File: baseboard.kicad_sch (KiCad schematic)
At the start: 50 parts, among them J10 LCD_CHAR, J11 SERVO2, J12 BME280, J13 UART1, J14 FAN, J15 UART2, J16 AS7265X, J17 TFT_SPI, J5 POWER, J6 DCMI_CAMERA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

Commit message: snapshot
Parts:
- removed J17: TFT_SPI, Connector_PinHeader_2.54mm:PinHeader_1x15_P2.54mm_Vertical, symbol EggClassifier:Conn_01x15
- added J17: TFT_SPI, EggClassifier:PinSocket_1x14_P2.54mm_Vertical, symbol LM2676S-3.3_NOPB:Conn_01x14
- C1, C3, C4: footprint Capacitor_THT:CP_Radial_D8.0mm_P3.50mm -> EggClassifier:CP_Radial_D8.0mm_P3.50mm_Hole1.0mm
- C10, C11, C2, C5, C6, C7, C8, C9: footprint Capacitor_SMD:C_0805_2012Metric_Pad1.18x1.45mm_HandSolder -> EggClassifier:C_0805_2012Metric_Pad1.18x1.45mm_HandSolder
- D1: footprint Diode_SMD:D_SMB_Handsoldering -> EggClassifier:D_SMB_Handsoldering
- D2, D3, D4: footprint Diode_SMD:D_SMA_Handsoldering -> EggClassifier:D_SMA_Handsoldering
- D5: footprint LED_SMD:LED_0805_2012Metric_Pad1.15x1.40mm_HandSolder -> EggClassifier:LED_0805_2012Metric_Pad1.15x1.40mm_HandSolder
- H1, H2, H3, H4: footprint PCM_JLCPCB:Hole, 3mm -> EggClassifier:Hole, 3mm
- J10, J12, J16, J5: footprint Connector_PinHeader_2.54mm:PinHeader_1x04_P2.54mm_Vertical -> EggClassifier:PinHeader_1x04_P2.54mm_Vertical
- J11, J13, J14, J15, J8, J9: footprint Connector_PinHeader_2.54mm:PinHeader_1x03_P2.54mm_Vertical -> EggClassifier:PinHeader_1x03_P2.54mm_Vertical
- J6: footprint Connector_PinHeader_2.54mm:PinHeader_2x09_P2.54mm_Vertical -> EggClassifier:PinHeader_2x09_P2.54mm_Vertical
- J7: footprint Connector_PinHeader_2.54mm:PinHeader_2x05_P2.54mm_Vertical -> EggClassifier:PinHeader_2x05_P2.54mm_Vertical
- L1: footprint JLCPCB:L_SMD,8x8mm -> EggClassifier:L_SMD,8x8mm
- Q1, Q2, Q3: footprint PCM_Package_TO_SOT_SMD_AKL:SOT-223-3_TabPin2 -> EggClassifier:SOT-223-3_TabPin2
- R1, R10, R11, R2, R3, R4, R5, R6, R7, R8, R9: footprint Resistor_SMD:R_0805_2012Metric_Pad1.20x1.40mm_HandSolder -> EggClassifier:R_0805_2012Metric_Pad1.20x1.40mm_HandSolder
- U1: footprint LM2676S-3.3_NOPB:TO127P1435X464-8N -> EggClassifier:TO127P1435X464-8N
- U2: footprint Package_TO_SOT_SMD:SOT-223-3_TabPin2 -> EggClassifier:SOT-223-3_TabPin2
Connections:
- net GND: now also J17.2 (Pin_2); no longer J7.9 (Pin_9)
- net SPI1_MISO: now also J17.13 (Pin_13)
- net SPI1_MOSI: now also J17.12 (Pin_12)
- net SPI1_NCS: now also J17.11 (Pin_11)
- net SPI1_SCK: now also J17.10 (Pin_10)
- net SPI2_MISO: now also J17.9 (Pin_9)
- net SPI2_MOSI: now also J17.6 (Pin_6)
- net SPI2_NCS: now also J17.3 (Pin_3)
- net SPI2_SCK: now also J17.7 (Pin_7)
- net TFT_BL: now also J17.8 (Pin_8)
- net TFT_INT: now also J17.14 (Pin_14)
- net TFT_RS: now also J17.5 (Pin_5)
- net VCC: now also J7.9 (Pin_9), J17.1 (Pin_1)
- net at R11.2: now also J17.4 (Pin_4)

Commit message: yet more tweaks
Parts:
- J5: footprint EggClassifier:PinHeader_1x04_P2.54mm_Vertical -> EggClassifier:TerminalBlock_Xinya_XY308-2.54-4P_1x04_P2.54mm_Horizontal
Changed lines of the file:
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@@
 			)
 		)
-		(property "Footprint" "EggClassifier:PinHeader_1x04_P2.54mm_Vertical"
+		(property "Footprint" "EggClassifier:TerminalBlock_Xinya_XY308-2.54-4P_1x04_P2.54mm_Horizontal"
 			(at 25.4 133.35 0)
 			(effects

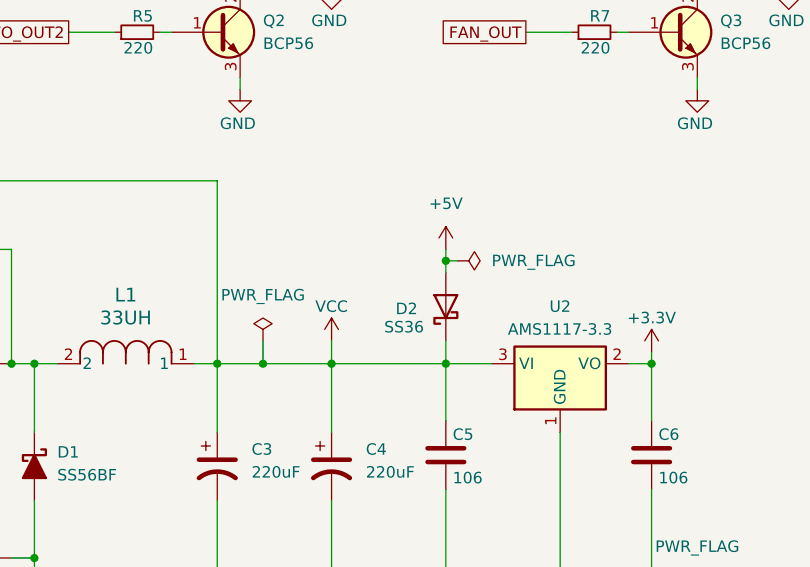
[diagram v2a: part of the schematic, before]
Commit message: change board to dimensions 120mm x 80mm
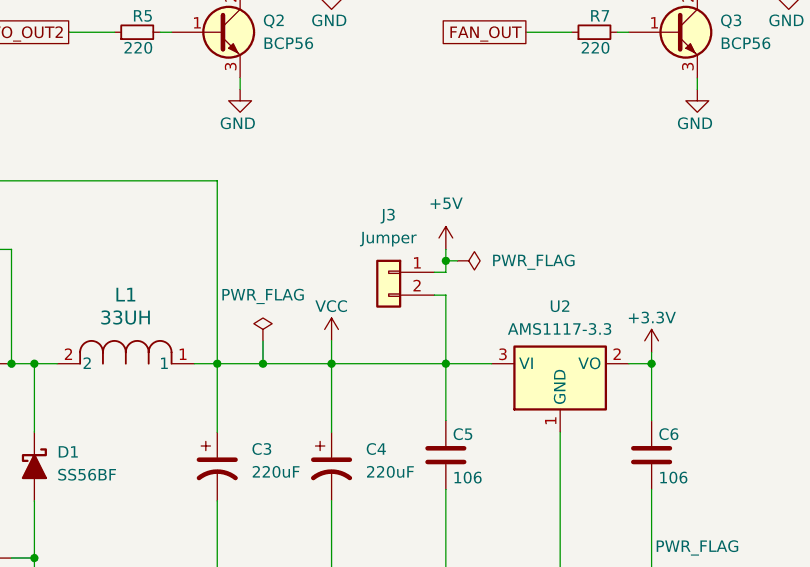
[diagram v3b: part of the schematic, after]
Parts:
- removed D2: SS36, EggClassifier:D_SMA_Handsoldering, symbol EggClassifier:SS36
- added J3: Jumper, Connector_PinSocket_2.54mm:PinSocket_1x02_P2.54mm_Vertical, symbol Connector_Generic:Conn_01x02
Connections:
- net +5V: now also J3.1 (Pin_1)
- net VCC: now also J3.2 (Pin_2)
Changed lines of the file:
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@@
 	(wire
 		(pts
+			(xy 144.78 125.73) (xy 146.05 125.73)
+		)
+		(stroke
+			(width 0)
+			(type default)
+		)
+	)
+	(wire
+		(pts
 			(xy 190.5 62.23) (xy 191.77 62.23)
 		)
@@
 	(wire
 		(pts
+			(xy 144.78 128.27) (xy 146.05 128.27)
+		)
+		(stroke
+			(width 0)
+			(type default)
+		)
+	)
+	(wire
+		(pts
 			(xy 190.5 24.13) (xy 190.5 25.4)
 		)
@@
 	(wire
 		(pts
-			(xy 146.05 133.35) (xy 146.05 135.89)
+			(xy 146.05 128.27) (xy 146.05 135.89)
 		)
 		(stroke
@@
 	)
 	(symbol
-		(lib_id "EggClassifier:SS36")
-		(at 146.05 129.54 90)
-		(unit 1)
-		(exclude_from_sim no)
-		(in_bom yes)
-		(on_board yes)
-		(dnp no)
-		(property "Reference" "D2"
-			(at 140.462 129.794 90)
-			(effects
-				(font
-					(size 1.27 1.27)
-				)
-				(justify right)
-			)
-		)
-		(property "Value" "SS36"
-			(at 139.192 131.826 90)
-			(effects
-				(font
-					(size 1.27 1.27)
-				)
-				(justify right)
-			)
-		)
-		(property "Footprint" "EggClassifier:D_SMA_Handsoldering"
-			(at 150.495 129.54 0)
-			(effects
-				(font
-					(size 1.27 1.27)
-				)
-				(hide yes)
-			)
-		)
-		(property "Datasheet" "https://www.vishay.com/docs/88751/ss32.pdf"
-			(at 146.05 129.54 0)
-			(effects
-				(font
-					(size 1.27 1.27)
-				)
-				(hide yes)
-			)
-		)
-		(property "Description" "60V 3A Schottky Diode, SMA"
-			(at 146.05 129.54 0)
-			(effects
-				(font
-					(size 1.27 1.27)
-				)
-				(hide yes)
-			)
-		)
-		(pin "1"
-		)
-		(pin "2"
-		)
-		(instances
-			(project "Main_H743VI"
-				(path "/1c72d2eb-7fb1-49fe-a026-e817f5a7ec43/16aff487-3924-4be3-b176-d1fab0e3868e"
-					(reference "D2")
-					(unit 1)
-				)
-			)
-		)
-	)
-	(symbol
 		(lib_id "EggClassifier:Conn_01x03")
 		(at 196.85 62.23 0)
@@
 					(unit 1)
 				)
+			)
+		)
+	)
+	(symbol
+		(lib_id "Connector_Generic:Conn_01x02")
+		(at 139.7 125.73 0)
+		(mirror y)
+		(unit 1)
+		(exclude_from_sim no)
+		(in_bom yes)
+		(on_board yes)
+		(dnp no)
+		(fields_autoplaced yes)
+		(property "Reference" "J3"
+			(at 139.7 119.38 0)
+			(effects
+				(font
+					(size 1.27 1.27)
+				)
+			)
+		)
+		(property "Value" "Jumper"
+			(at 139.7 121.92 0)
+			(effects
+				(font
+					(size 1.27 1.27)
+				)
+			)
+		)
+		(property "Footprint" "Connector_PinSocket_2.54mm:PinSocket_1x02_P2.54mm_Vertical"
+			(at 139.7 125.73 0)
+			(effects
+				(font
+					(size 1.27 1.27)
+				)
+				(hide yes)
+			)
+		)
+		(property "Datasheet" "~"
+			(at 139.7 125.73 0)
+			(effects
+				(font
+					(size 1.27 1.27)
+				)
+				(hide yes)
+			)
+		)
+		(property "Description" "Generic connector, single row, 01x02, script generated (kicad-library-utils/schlib/autogen/connector/)"
+			(at 139.7 125.73 0)
+			(effects
+				(font
+					(size 1.27 1.27)
+				)
+				(hide yes)
+			)
+		)
+		(pin "1"
+		)
+		(pin "2"
+		)
+		(instances
+			(project ""
+				(path "/1c72d2eb-7fb1-49fe-a026-e817f5a7ec43/16aff487-3924-4be3-b176-d1fab0e3868e"
+					(reference "J3")
+					(unit 1)
+				)

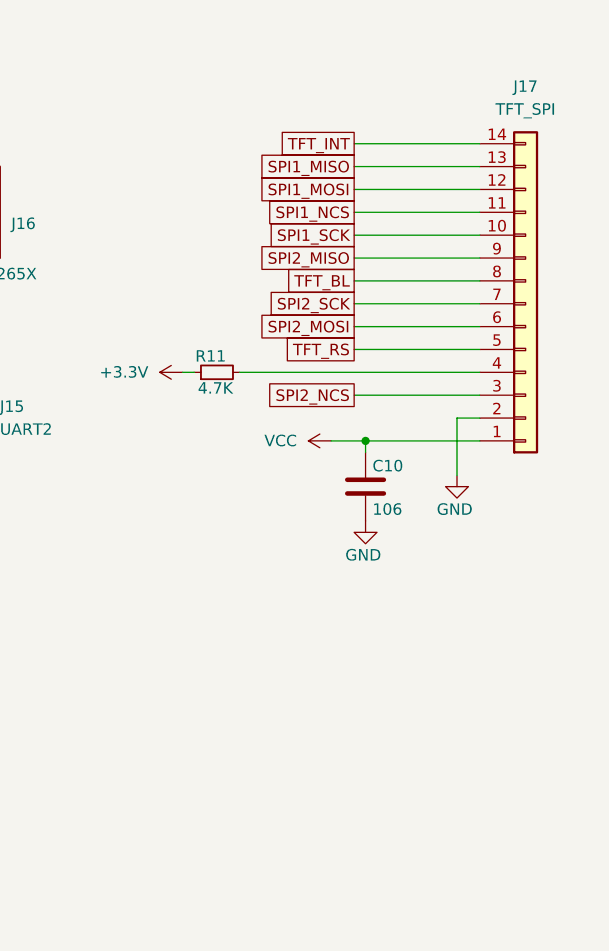
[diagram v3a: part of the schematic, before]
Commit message: finished layout;. H743 with SD-Card
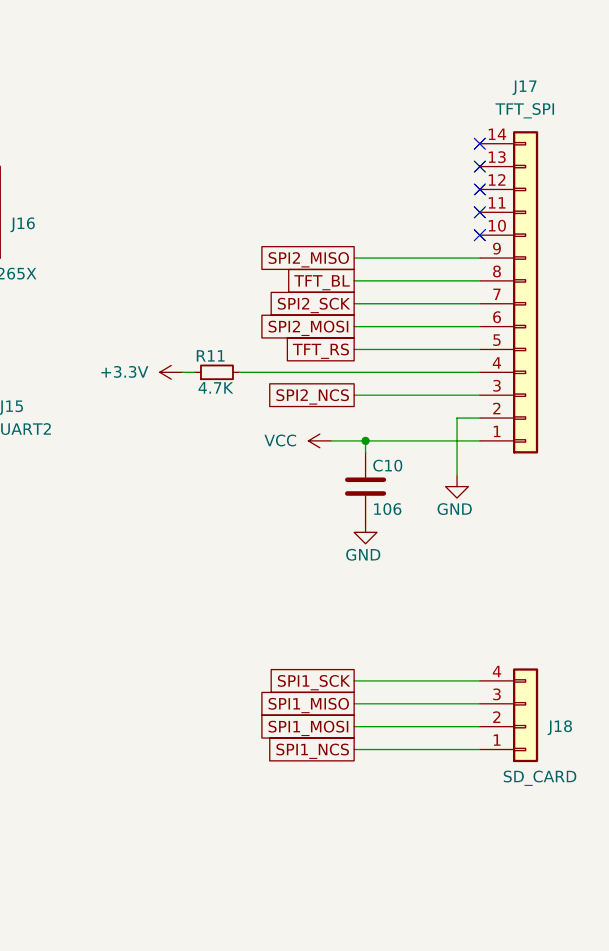
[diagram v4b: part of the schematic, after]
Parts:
- added J18: SD_CARD, EggClassifier:PinHeader_1x04_P2.54mm_Vertical, symbol EggClassifier:Conn_01x04
- J3: footprint Connector_PinSocket_2.54mm:PinSocket_1x02_P2.54mm_Vertical -> Connector_PinHeader_2.54mm:PinHeader_1x02_P2.54mm_Vertical
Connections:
- net SPI1_MISO: now also J18.3 (Pin_3); no longer J17.13 (Pin_13)
- net SPI1_MOSI: now also J18.2 (Pin_2); no longer J17.12 (Pin_12)
- net SPI1_NCS: now also J18.1 (Pin_1); no longer J17.11 (Pin_11)
- net SPI1_SCK: now also J18.4 (Pin_4); no longer J17.10 (Pin_10)
- net TFT_INT: no longer names the net of J17.14 (Pin_14)
- no-connect marks 2 -> 7
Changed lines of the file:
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@@
 	)
 	(no_connect
+		(at 252.73 39.37)
+	)
+	(no_connect
+		(at 252.73 36.83)
+	)
+	(no_connect
 		(at 62.23 151.13)
 	)
@@
 		(at 62.23 156.21)
 	)
+	(no_connect
+		(at 252.73 31.75)
+	)
+	(no_connect
+		(at 252.73 34.29)
+	)
+	(no_connect
+		(at 252.73 41.91)
+	)
 	(wire
 		(pts
@@
 	(wire
 		(pts
-			(xy 252.73 41.91) (xy 238.76 41.91)
+			(xy 252.73 91.44) (xy 238.76 91.44)
 		)
 		(stroke
@@
 	(wire
 		(pts
-			(xy 252.73 31.75) (xy 238.76 31.75)
-		)
-		(stroke
-			(width 0)
-			(type default)
-		)
-	)
-	(wire
-		(pts
 			(xy 173.99 83.82) (xy 184.15 83.82)
 		)
@@
 	(wire
 		(pts
-			(xy 252.73 36.83) (xy 238.76 36.83)
+			(xy 252.73 96.52) (xy 238.76 96.52)
 		)
 		(stroke
@@
 	(wire
 		(pts
-			(xy 252.73 34.29) (xy 238.76 34.29)
+			(xy 252.73 93.98) (xy 238.76 93.98)
 		)
 		(stroke
@@
 	(wire
 		(pts
-			(xy 252.73 39.37) (xy 238.76 39.37)
+			(xy 252.73 99.06) (xy 238.76 99.06)
 		)
 		(stroke
@@
 	(global_label "SPI1_MISO"
 		(shape passive)
-		(at 238.76 34.29 180)
+		(at 238.76 93.98 180)
 		(fields_autoplaced yes)
 		(effects
@@
 		)
 		(property "Intersheetrefs" "${INTERSHEET_REFS}"
-			(at 227.0285 34.29 0)
+			(at 227.0285 93.98 0)
 			(effects
 				(font
@@
 	(global_label "SPI1_SCK"
 		(shape passive)
-		(at 238.76 41.91 180)
+		(at 238.76 91.44 180)
 		(fields_autoplaced yes)
 		(effects
@@
 		)
 		(property "Intersheetrefs" "${INTERSHEET_REFS}"
-			(at 227.8752 41.91 0)
+			(at 227.8752 91.44 0)
 			(effects
 				(font
@@
 	(global_label "SPI1_MOSI"
 		(shape passive)
-		(at 238.76 36.83 180)
+		(at 238.76 96.52 180)
 		(fields_autoplaced yes)
 		(effects
@@
 		)
 		(property "Intersheetrefs" "${INTERSHEET_REFS}"
-			(at 227.0285 36.83 0)
+			(at 227.0285 96.52 0)
 			(effects
 				(font
@@
 		)
 	)
-	(global_label "TFT_INT"
-		(shape passive)
-		(at 238.76 31.75 180)
-		(fields_autoplaced yes)
-		(effects
-			(font
-				(size 1.27 1.27)
-			)
-			(justify right)
-		)
-		(property "Intersheetrefs" "${INTERSHEET_REFS}"
-			(at 229.9918 31.75 0)
-			(effects
-				(font
-					(size 1.27 1.27)
-				)
-				(justify right)
-				(hide yes)
-			)
-		)
-	)
 	(global_label "TFT_RS"
 		(shape passive)
@@
 	(global_label "SPI1_NCS"
 		(shape passive)
-		(at 238.76 39.37 180)
+		(at 238.76 99.06 180)
 		(fields_autoplaced yes)
 		(effects
@@
 		)
 		(property "Intersheetrefs" "${INTERSHEET_REFS}"
-			(at 227.8147 39.37 0)
+			(at 227.8147 99.06 0)
 			(effects
 				(font
@@
 	)
 	(symbol
+		(lib_id "EggClassifier:Conn_01x04")
+		(at 257.81 96.52 0)
+		(mirror x)
+		(unit 1)
+		(exclude_from_sim no)
+		(in_bom yes)
+		(on_board yes)
+		(dnp no)
+		(property "Reference" "J18"
+			(at 260.35 96.5201 0)
+			(effects
+				(font
+					(size 1.27 1.27)
+				)
+				(justify left)
+			)
+		)
+		(property "Value" "SD_CARD"
+			(at 255.27 102.108 0)
+			(effects
+				(font
+					(size 1.27 1.27)
+				)
+				(justify left)
+			)
+		)
+		(property "Footprint" "EggClassifier:PinHeader_1x04_P2.54mm_Vertical"
+			(at 257.81 96.52 0)
+			(effects
+				(font
+					(size 1.27 1.27)
+				)
+				(hide yes)
+			)
+		)
+		(property "Datasheet" "~"
+			(at 257.81 96.52 0)
+			(effects
+				(font
+					(size 1.27 1.27)
+				)
+				(hide yes)
+			)
+		)
+		(property "Description" "Generic connector, single row, 01x04, script generated (kicad-library-utils/schlib/autogen/connector/)"
+			(at 257.81 96.52 0)
+			(effects
+				(font
+					(size 1.27 1.27)
+				)
+				(hide yes)
+			)
+		)
+		(pin "1"
+		)
+		(pin "2"
+		)
+		(pin "3"
+		)
+		(pin "4"
+		)
+		(instances
+			(project "EggClassifier"
+				(path "/1c72d2eb-7fb1-49fe-a026-e817f5a7ec43/16aff487-3924-4be3-b176-d1fab0e3868e"
+					(reference "J18")
+					(unit 1)
+				)
+			)
+		)
+	)
+	(symbol
 		(lib_id "LM2676S-3.3_NOPB:+3.3V")
 		(at 33.02 130.81 270)
@@
 			)
 		)
-		(property "Footprint" "Connector_PinSocket_2.54mm:PinSocket_1x02_P2.54mm_Vertical"
+		(property "Footprint" "Connector_PinHeader_2.54mm:PinHeader_1x02_P2.54mm_Vertical"
 			(at 139.7 125.73 0)
 			(effects

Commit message: end of day snapshot
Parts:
- J10, J11, J12, J13, J14, J15, J16, J17, J3, J5, J6, J7, J8, J9: now left out of the parts list
- J18: footprint EggClassifier:PinHeader_1x04_P2.54mm_Vertical -> Connector_PinSocket_2.54mm:PinSocket_1x04_P2.54mm_Vertical; now left out of the parts list
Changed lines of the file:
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@@
 		(unit 1)
 		(exclude_from_sim no)
-		(in_bom yes)
+		(in_bom no)
 		(on_board yes)
 		(dnp no)
@@
 		(unit 1)
 		(exclude_from_sim no)
-		(in_bom yes)
+		(in_bom no)
 		(on_board yes)
 		(dnp no)
@@
 		(unit 1)
 		(exclude_from_sim no)
-		(in_bom yes)
+		(in_bom no)
 		(on_board yes)
 		(dnp no)
@@
 		(unit 1)
 		(exclude_from_sim no)
-		(in_bom yes)
+		(in_bom no)
 		(on_board yes)
 		(dnp no)
@@
 		(unit 1)
 		(exclude_from_sim no)
-		(in_bom yes)
+		(in_bom no)
 		(on_board yes)
 		(dnp no)
@@
 		(unit 1)
 		(exclude_from_sim no)
-		(in_bom yes)
+		(in_bom no)
 		(on_board yes)
 		(dnp no)
@@
 		(unit 1)
 		(exclude_from_sim no)
-		(in_bom yes)
+		(in_bom no)
 		(on_board yes)
 		(dnp no)
@@
 		(unit 1)
 		(exclude_from_sim no)
-		(in_bom yes)
+		(in_bom no)
 		(on_board yes)
 		(dnp no)
@@
 		(unit 1)
 		(exclude_from_sim no)
-		(in_bom yes)
+		(in_bom no)
 		(on_board yes)
 		(dnp no)
@@
 		(unit 1)
 		(exclude_from_sim no)
-		(in_bom yes)
+		(in_bom no)
 		(on_board yes)
 		(dnp no)
@@
 		(unit 1)
 		(exclude_from_sim no)
-		(in_bom yes)
+		(in_bom no)
 		(on_board yes)
 		(dnp no)
@@
 		(unit 1)
 		(exclude_from_sim no)
-		(in_bom yes)
+		(in_bom no)
 		(on_board yes)
 		(dnp no)
@@
 		(unit 1)
 		(exclude_from_sim no)
-		(in_bom yes)
+		(in_bom no)
 		(on_board yes)
 		(dnp no)
@@
 			)
 		)
-		(property "Footprint" "EggClassifier:PinHeader_1x04_P2.54mm_Vertical"
+		(property "Footprint" "Connector_PinSocket_2.54mm:PinSocket_1x04_P2.54mm_Vertical"
 			(at 257.81 96.52 0)
 			(effects
@@
 		(unit 1)
 		(exclude_from_sim no)
-		(in_bom yes)
+		(in_bom no)
 		(on_board yes)
 		(dnp no)
@@
 		(unit 1)
 		(exclude_from_sim no)
-		(in_bom yes)
+		(in_bom no)
 		(on_board yes)
 		(dnp no)
